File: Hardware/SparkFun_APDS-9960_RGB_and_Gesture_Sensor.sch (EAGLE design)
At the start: 19 parts, among them U1 APDS-9960

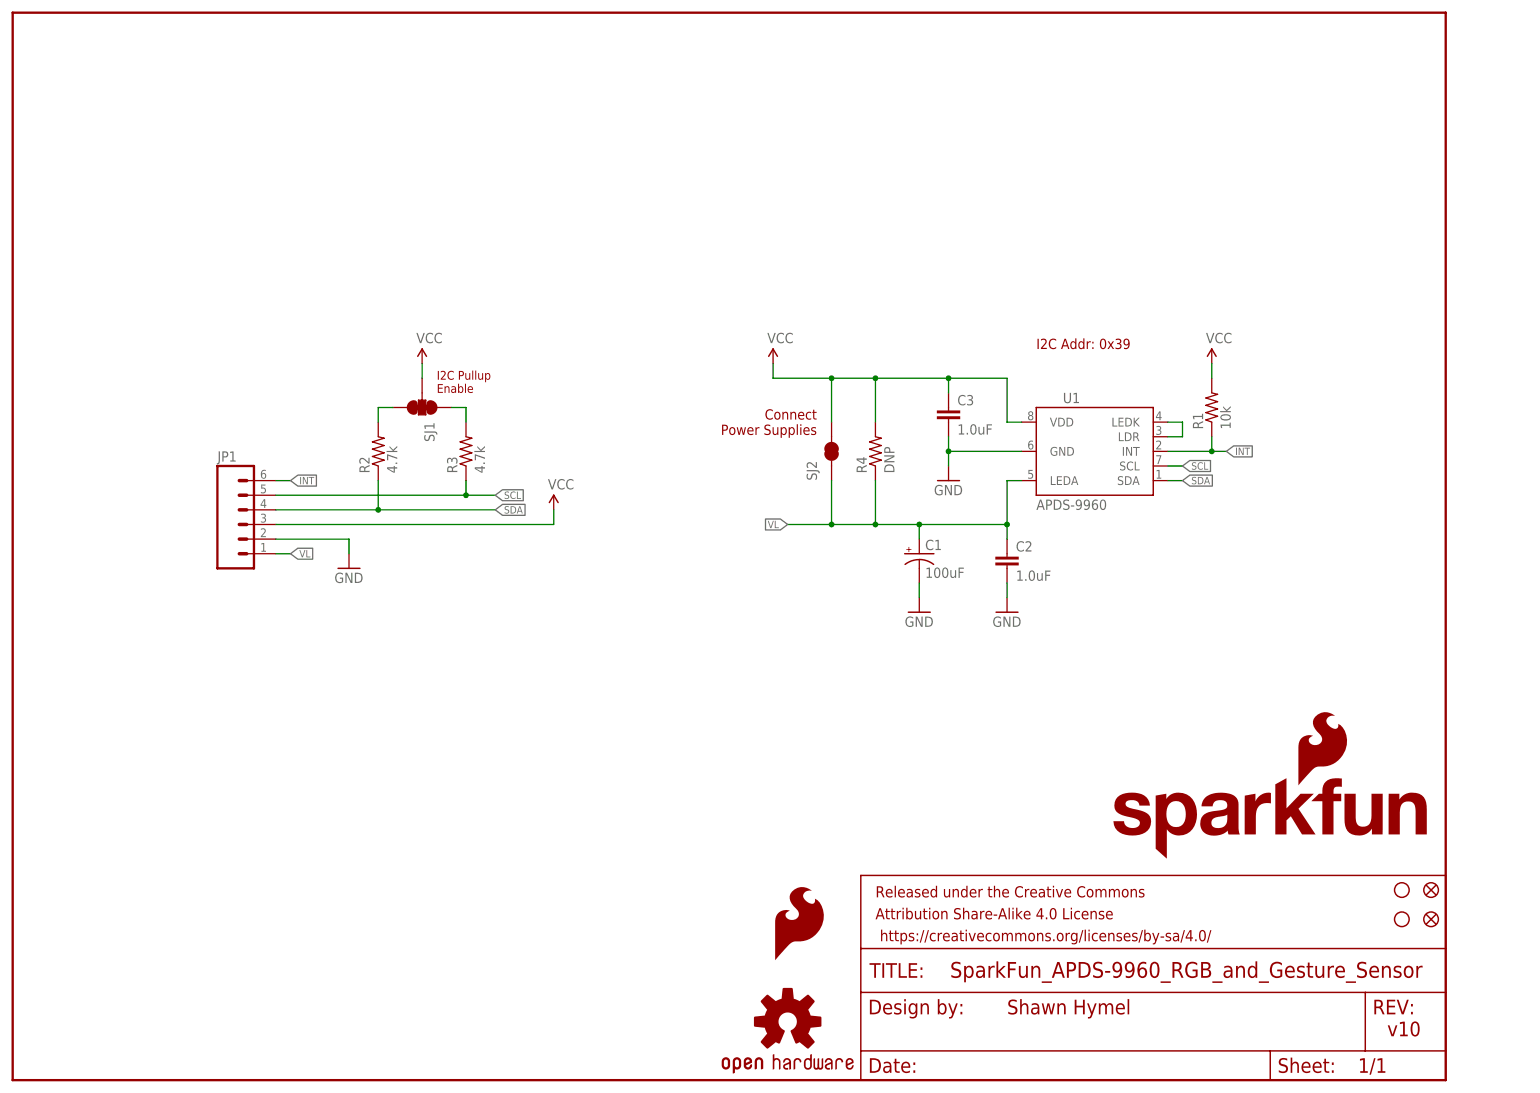
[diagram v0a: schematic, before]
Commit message: Suggestions For Possible Board Revision
I have a few suggestions to make this board work better in my
application.
I'm a noob with GitHub, so I appologise if I'm doing this wrong.

Changes:
1) Rotate and relocate sensor as close as possible to edge of board.
Reason: I want to be able to put this sensor board into an enclosure
next to an LCD. The sensor needs to be as close to the LCD for both to
fit in the window.

2) Add location on back of board for large electrolytic capacitor.
Reason: placing the capacitor behind the sensor improves packaging
options for the board and sensor.

3) Added voltage regulator and level shifting components to make the
board 5V safe.
Reason: Easier to integrate with Arduinos and other 5V micros.
Note: In my understanding of the APDS datasheet the sensor can pull up
to 790mA. Because of this, a 1A regulator was selected, MCP1826T. Device
and footprint created in my Eagle library
(https://github.com/akreager/ATK_Engineering-Eagle_Library). I2C level
shifter design "borrowed" from SparkFun logic level shifter board.

4) (Least important) Attempted to add provisions to be able to break
board into two pieces and reconnet with jumper wires.
Reason: Packaging.

5) Moved fiduciary marks and silkscreens, added mounting holes, changed
revision in the board to v10x1 (my way to signify an unapproved
revision).
Reason: clearance; revision tracking.
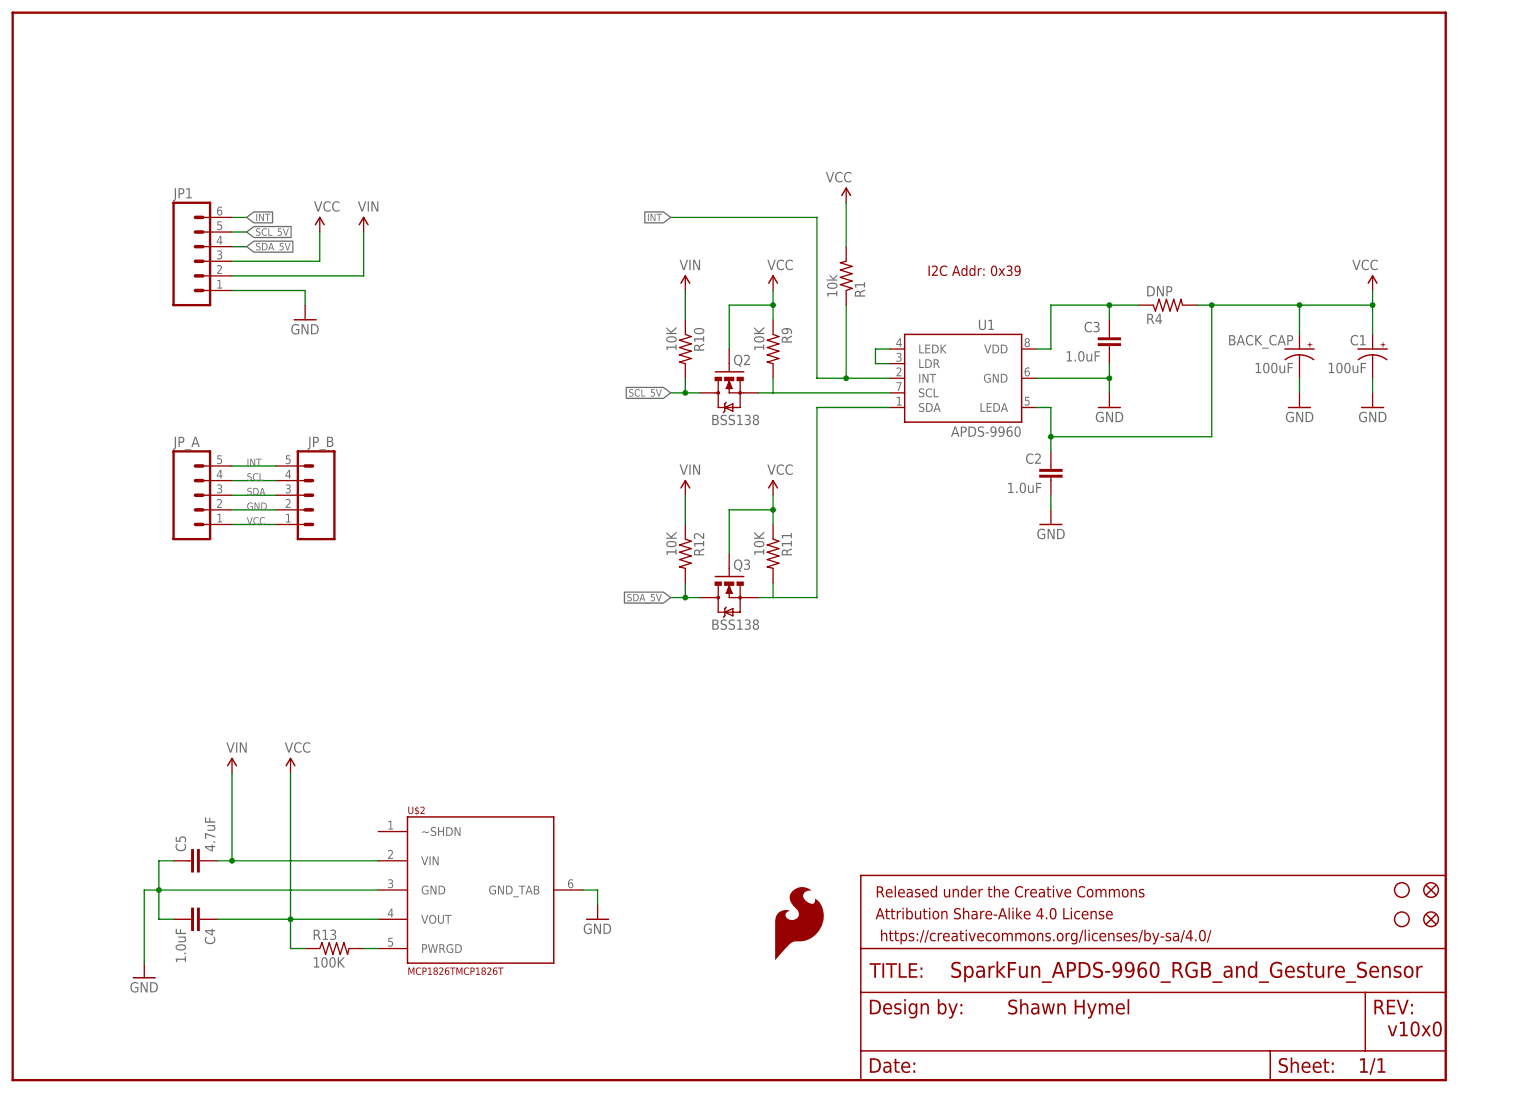
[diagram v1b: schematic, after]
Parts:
- removed LOGO2: OSHW-LOGOS, SparkFun-Aesthetics:OSHW-LOGOS
- removed R2, R3: 4.7k, SparkFun-Resistors:4.7KOHM1/10W1%(0603)
- removed SJ1: (no value), SparkFun-Passives:SOLDERJUMPER_2WAYPASTE1&2&3
- removed SJ2: SOLDERJUMPERNC, SparkFun-Retired:SOLDERJUMPERNC
- removed U$1: SFE_LOGO_NAME_FLAME.1_INCH, SparkFun-Aesthetics:SFE_LOGO_NAME_FLAME.1_INCH
- added BACK_CAP: 100uF, SparkFun-Capacitors:100UF-10V-10%(TANT)
- added C4: 1.0uF, SparkFun-Capacitors:1.0UF-16V-10%(0603)
- added C5: 4.7uF, SparkFun-Capacitors:1.0UF-16V-10%(0603)
- added JP_A, JP_B: (no value), SparkFun-Connectors:M05PTH
- added Q2, Q3: BSS138, SparkFun:MOSFET-NCHANNELSMD
- added R10, R11, R12, R9: 10K, SparkFun:RESISTOR0603-RES
- added R13: 100K, SparkFun:RESISTOR0603-RES
- added U$2: MCP1826TMCP1826T, ATK_lib:MCP1826TMCP1826T
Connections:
- removed net N$2: R3.2, SJ1.1
- removed net VL: C1.+, C2.1, JP1.1, R4.1, SJ2.1, U1.LEDA
- new net N$6: R13.2, U$2.PWRGD
- new net SCL_5V: JP1.5, Q2.D, R10.2
- new net SDA_5V: JP1.4, Q3.D, R12.2
- new net VIN: C5.2, JP1.2, R10.1, R12.1, U$2.VIN
- net GND: now also BACK_CAP.-, C4.2, C5.1, JP1.1, JP_A.2, JP_B.2, U$2.GND, U$2.GND_TAB; no longer JP1.2
- net INT: now also JP_A.5, JP_B.5
- net N$1: now also C3.1, R4.1, U1.VDD; no longer R2.2, SJ1.3
- net SCL: now also JP_A.4, JP_B.4, Q2.S, R9.2; no longer JP1.5, R3.1
- net SDA: now also JP_A.3, JP_B.3, Q3.S, R11.2; no longer JP1.4, R2.1
- net VCC: now also BACK_CAP.+, C1.+, C2.1, C4.1, JP_A.1, JP_B.1, Q2.G, Q3.G, R11.1, R13.1, R9.1, U$2.VOUT, U1.LEDA; no longer C3.1, SJ1.2, SJ2.2, U1.VDD
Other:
- note added: "v10x0"
- note removed: "Connect Power Supplies"
- note removed: "I2C Pullup Enable"
- note removed: "v10"
- moved on the sheet: C1, C2, C3, JP1, R1, R4, U1
